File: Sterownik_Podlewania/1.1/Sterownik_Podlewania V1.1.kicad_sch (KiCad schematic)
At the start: 28 parts, among them J3 RJ45, J4 Conn_01x04_Socket, J5 RJ45, J8 RJ45, U1 ESP32-DEVKITC, U11 757, U5 757

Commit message: Pociągnięcie prawie wszystkich ścieżek, dodanie rezystorów do I2C 5V
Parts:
- added R12, R14: 4k7, Resistor_SMD:R_1206_3216Metric, symbol Device:R
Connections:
- net +5V: now also R12.1, R14.1
- net DS_WYJŚCIE: now also U1.9 (IO25); no longer U1.12 (IO14)
- net SCL_5V: now also R14.2
- net SDA_5V: now also R12.2

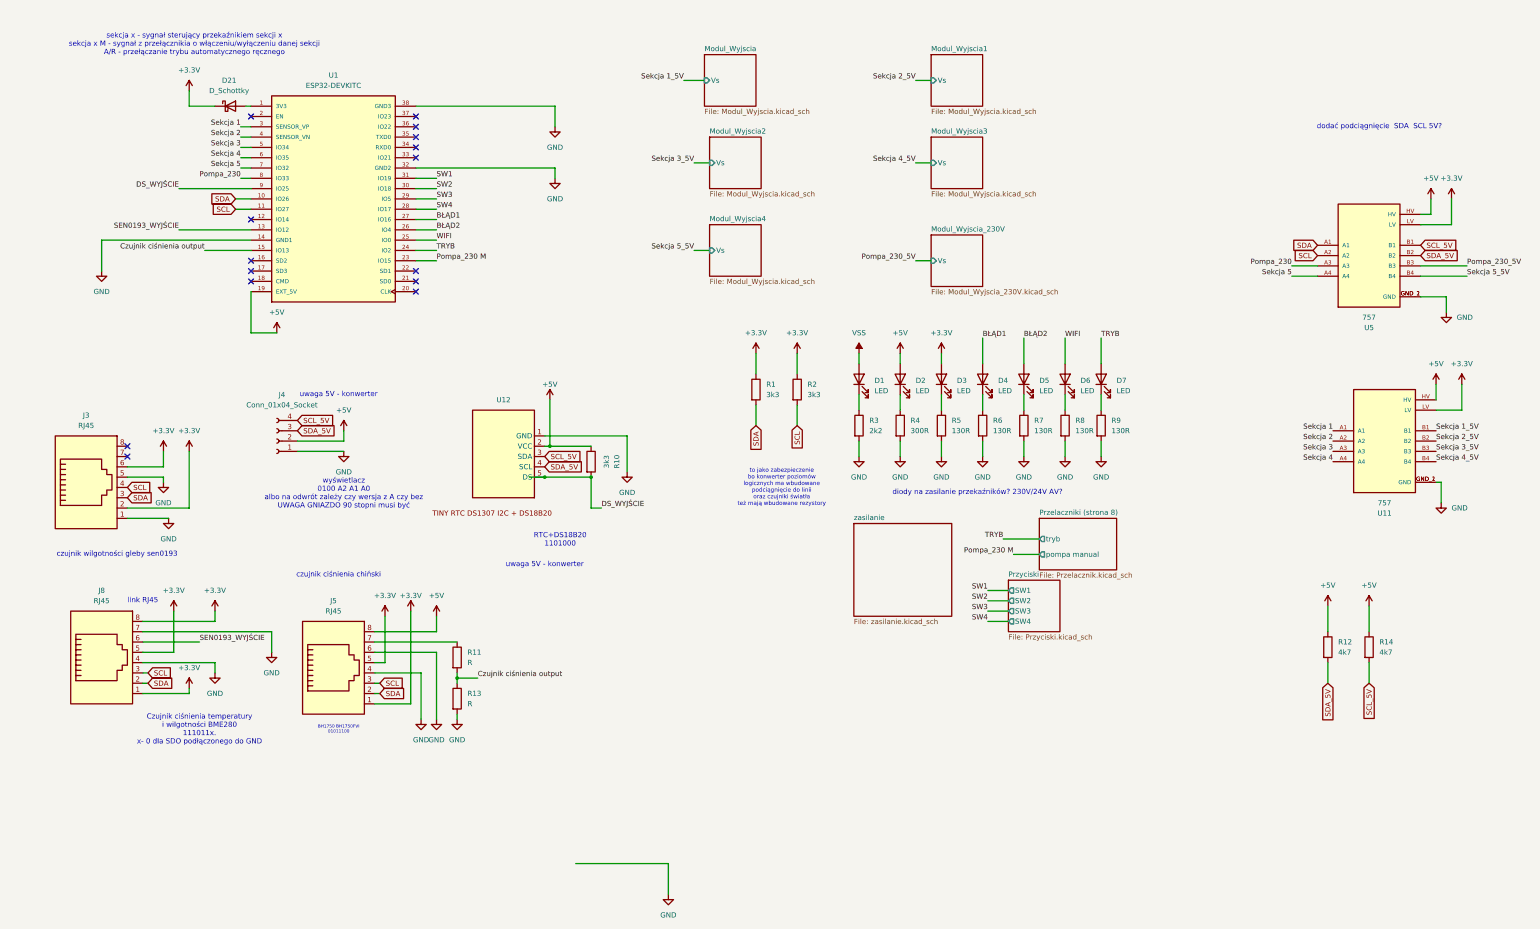
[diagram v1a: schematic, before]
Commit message: Poprawiono błędy połączeń SDA,SCL, dodno drugą magistralę I2C, pociągnięcie nowych ścieżek
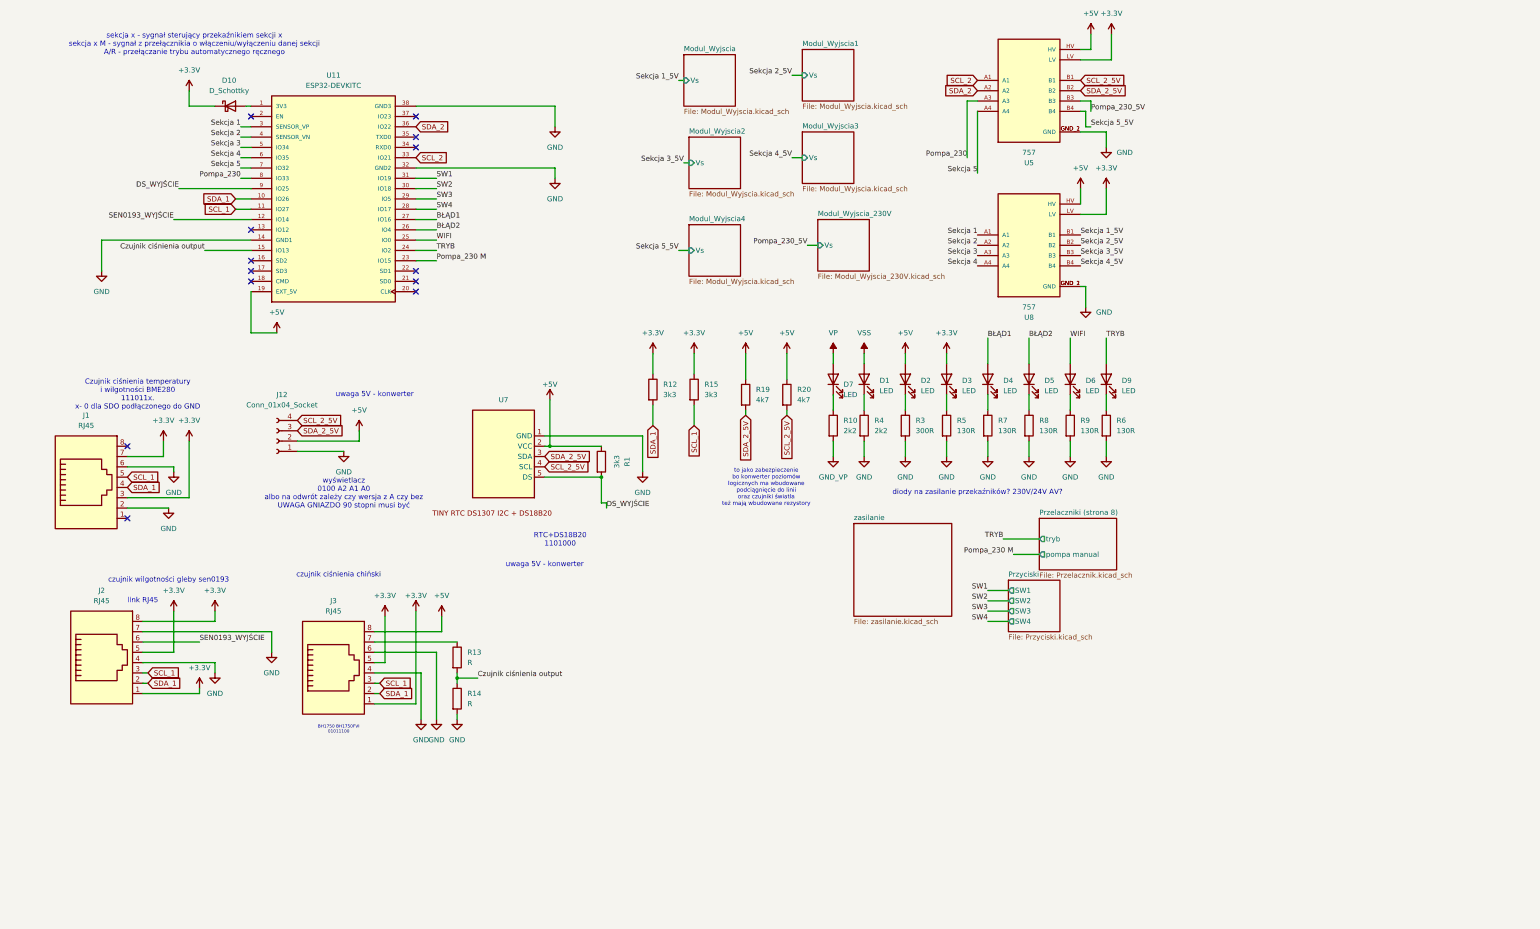
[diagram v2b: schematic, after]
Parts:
- removed U12: ~, RTC:RTC DS1307 + 32kb EEPROM 24C32 I2C, symbol RTC:TINY_RTC_DS1307
- added D7: LED, LED_SMD:LED_1206_3216Metric, symbol Device:LED
- added R10: 2k2, Resistor_SMD:R_1206_3216Metric, symbol Device:R
- added U7: ~, RTC:RTC DS1307 + 32kb EEPROM 24C32 I2C, symbol RTC:TINY_RTC_DS1307
- renumbered D21 to D10, D7 to D9, J3 to J1, J4 to J12, J8 to J2, J5 to J3, R10 to R1, R1 to R12, R11 to R13, R13 to R14, R2 to R15, R12 to R19, R14 to R20, R4 to R3, R3 to R4, R9 to R6, R6 to R7, R7 to R8, R8 to R9, U1 to U11, U11 to U8
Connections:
- net +3.3V: now also J1.3, J1.7; no longer J1.2, J1.6
- net +5V: now also U7.2 (VCC)
- net DS_WYJŚCIE: now also U7.5 (DS)
- net GND: now also J1.2, J1.6, U7.1 (GND); no longer J1.1, J1.5
- net SEN0193_WYJŚCIE: now also U11.12 (IO14); no longer U11.13 (IO12)
- net SCL_2: now reaches U11.33 (IO21)
- net SCL_2: now also U5.A1
- net SDA_2: now reaches U11.36 (IO22)
- net SDA_2: now also U5.A2
- net SCL renamed SCL_1
- net SCL_1: now also J1.5; no longer J1.4, U5.A2
- net SCL_5V renamed SCL_2_5V
- net SCL_2_5V: now also U7.4 (SCL)
- net SDA renamed SDA_1
- net SDA_1: now also J1.4; no longer J1.3, U5.A1
- net SDA_5V renamed SDA_2_5V
- net SDA_2_5V: now also U7.3 (SDA)
- new net: D7.1 (K), R10.1
- new net GND_VP: R10.2
- new net VP: D7.2 (A)
- no-connect marks 15 -> 13
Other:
- note removed: "dodać podciągnięcie SDA SCL 5V?"
- moved on the sheet: D1, D2, D3, D4, D5, D6, D9, R1, R12, R15, R19, R20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

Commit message: Poprawki schematu modułu zaworu, usunięcie przekaźnika, przygotowanie schematu zasilania
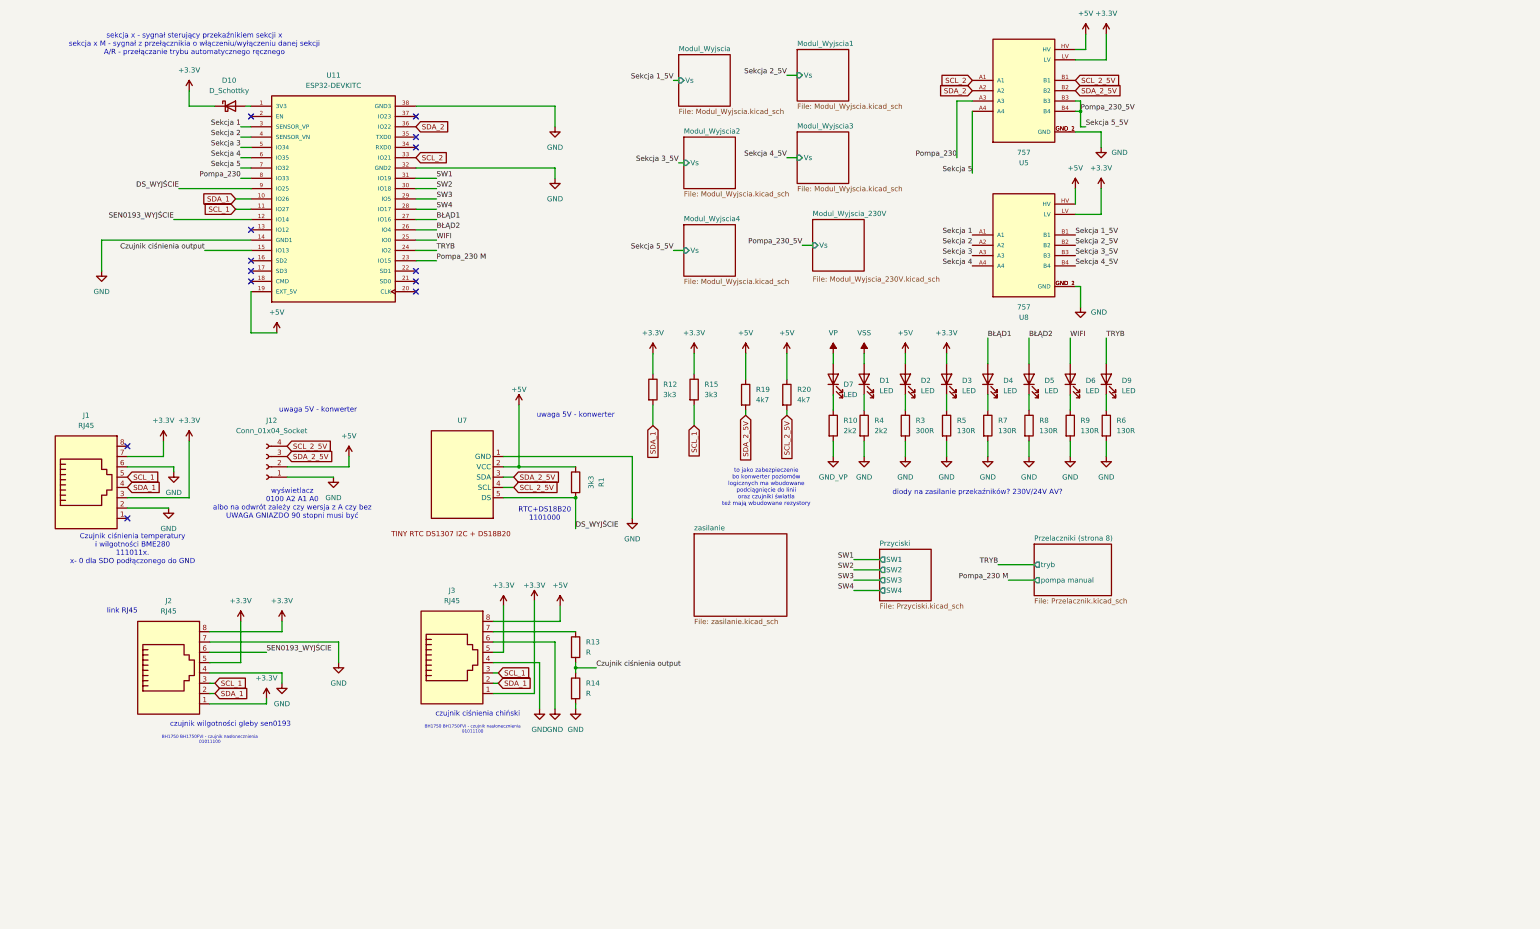
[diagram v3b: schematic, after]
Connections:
- net Sekcja 5_5V is gone; now on net Pompa_230_5V: U5.B4
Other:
- note added: "BH1750 BH1750FVI - czujnik nasłonecznienia 01011100"
- note removed: "BH1750 BH1750FVI 01011100"
- moved on the sheet: J12, J2, J3, R1, R13, R14, U5, U7, U8

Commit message: Usunięcie zewnętrzego zasilania 12 i stabilizatora napięcia, korekcja zasilania wzmacniacz operacyjny moduł zasilania
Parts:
- removed D1: LED, LED_SMD:LED_1206_3216Metric, symbol Device:LED
- removed R4: 2k2, Resistor_SMD:R_1206_3216Metric, symbol Device:R
- renumbered D10 to D1, D2 to D1, D4 to D2, D3 to D2, D5 to D4, D6 to D5, D7 to D6, D9 to D8, J12 to J3, J3 to J4, R5 to R10, R7 to R11, R8 to R12, R9 to R13, R6 to R14, R13 to R2, R14 to R3, R12 to R4, R15 to R5, R19 to R6, R20 to R7, R10 to R8, R3 to R9, U11 to U1, U7 to U2, U5 to U3, U8 to U4
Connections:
- net Pompa_230_5V: no longer U3.B4
- new net Sekcja 5_5V: U3.B4
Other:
- note added: "BH1750 BH1750FVI - czujnik światła I2C 01011100"
- note added: "to jako ewentualnosć do przytlutowania bo konwerter poziomów logicznych ma wbudowane podciągnięcie do linii oraz czujniki światła też mają wbudowane rezystory"
- note removed: "BH1750 BH1750FVI - czujnik nasłonecznienia 01011100"
- note removed: "to jako zabezpieczenie bo konwerter poziomów logicznych ma wbudowane podciągnięcie do linii oraz czujniki światła też mają wbudowane rezystory"
- moved on the sheet: D1, D2, D4, D5, D6, D8, R10, R11, R12, R13, R14, R8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

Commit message: Werja plików podesłana Mariuszkowi, dodane opisy i numeracja poprawna dla steronwika, w module poprawniono opis złącze ethernet
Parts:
- renumbered D8 to D11, D1 to D3, D2 to D6, D4 to D7, D5 to D8, D6 to D9, J3 to J12, J1 to J7, J2 to J8, J4 to J9, R9 to R1, R6 to R10, R7 to R11, R4 to R12, R5 to R13, R3 to R14, R2 to R15, R10 to R2, R11 to R3, R12 to R4, R13 to R5, R8 to R6, R14 to R8, R1 to R9, U1 to U10, U3 to U7, U2 to U8, U4 to U9
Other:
- note added: "sygnał manulanego włączenia pompy za pomocą przełącznika"
- note added: "tryb - ręczny/automatyczny"
- note removed: "diody na zasilanie przekaźników? 230V/24V AV?"
- note removed: "sekcja x - sygnał sterujący przekaźnikiem sekcji x sekcja x M - sygnał z przełącznikia o włączeniu/wyłączeniu danej sekcji A/R - przełączanie trybu automatycznego ręcznego"
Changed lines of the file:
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@@
 		)
 	)
-	(text "sekcja x - sygnał sterujący przekaźnikiem sekcji x\nsekcja x M - sygnał z przełącznikia o włączeniu/wyłączeniu danej sekcji\nA/R - przełączanie trybu automatycznego ręcznego"
+	(text "czujnik wilgotności gleby sen0193\n"
 		(exclude_from_sim no)
-		(at 50.8 21.59 0)
+		(at 59.69 189.23 0)
 		(effects
 			(font
 				(size 1.27 1.27)
 			)
+			(href "https://botland.com.pl/gravity-czujniki-pogodowe/10305-dfrobot-gravity-analogowy-czujnik-wilgotnosci-gleby-odporny-na-korozje-sen0193-6959420910434.html")
 		)
 	)
-	(text "czujnik wilgotności gleby sen0193\n"
+	(text "sygnał manulanego włączenia pompy\nza pomocą przełącznika\n"
 		(exclude_from_sim no)
-		(at 59.69 189.23 0)
+		(at 130.81 77.47 0)
 		(effects
 			(font
 				(size 1.27 1.27)
 			)
-			(href "https://botland.com.pl/gravity-czujniki-pogodowe/10305-dfrobot-gravity-analogowy-czujnik-wilgotnosci-gleby-odporny-na-korozje-sen0193-6959420910434.html")
 		)
 	)
-	(text "diody na zasilanie przekaźników? 230V/24V AV?"
+	(text "tryb - ręczny/automatyczny"
 		(exclude_from_sim no)
-		(at 243.84 132.08 0)
+		(at 130.81 71.12 0)
 		(effects
 			(font
@@
 	(text "to jako ewentualnosć do przytlutowania\nbo konwerter poziomów\nlogicznych ma wbudowane \npodciągnięcie do linii \noraz czujniki światła \nteż mają wbudowane rezystory"
 		(exclude_from_sim no)
-		(at 190.5 130.81 0)
+		(at 189.23 132.08 0)
 		(effects
 			(font
@@
 		(dnp no)
 		(fields_autoplaced yes)
-		(property "Reference" "D4"
+		(property "Reference" "D7"
 			(at 259.08 104.4574 90)
 			(effects
@@
 			(project "Sterownik_Podlewania"
 				(path "/a66bdf1f-0e2a-4cc5-beb1-605f2a3b9885"
-					(reference "D4")
+					(reference "D7")
 					(unit 1)
 				)
@@
 		(dnp no)
 		(fields_autoplaced yes)
-		(property "Reference" "R7"
+		(property "Reference" "R11"
 			(at 199.39 106.6799 0)
 			(effects
@@
 			(project "Sterownik_Podlewania V1.1"
 				(path "/a66bdf1f-0e2a-4cc5-beb1-605f2a3b9885"
-					(reference "R7")
+					(reference "R11")
 					(unit 1)
 				)
@@
 		(dnp no)
 		(fields_autoplaced yes)
-		(property "Reference" "J1"
+		(property "Reference" "J7"
 			(at 24.13 113.03 0)
 			(effects
@@
 			(project "Sterownik_Podlewania"
 				(path "/a66bdf1f-0e2a-4cc5-beb1-605f2a3b9885"
-					(reference "J1")
+					(reference "J7")
 					(unit 1)
 				)
@@
 		(on_board yes)
 		(dnp no)
-		(property "Reference" "J3"
+		(property "Reference" "J12"
 			(at 69.85 114.3 0)
 			(effects
@@
 			(project ""
 				(path "/a66bdf1f-0e2a-4cc5-beb1-605f2a3b9885"
-					(reference "J3")
+					(reference "J12")
 					(unit 1)
 				)
@@
 		(on_board yes)
 		(dnp no)
-		(property "Reference" "R1"
+		(property "Reference" "R9"
 			(at 151.13 129.54 90)
 			(effects
@@
 			(project ""
 				(path "/a66bdf1f-0e2a-4cc5-beb1-605f2a3b9885"
-					(reference "R1")
+					(reference "R9")
 					(unit 1)
 				)
@@
 		(dnp no)
 		(fields_autoplaced yes)
-		(property "Reference" "R14"
+		(property "Reference" "R8"
 			(at 276.86 114.2999 0)
 			(effects
@@
 			(project "Sterownik_Podlewania"
 				(path "/a66bdf1f-0e2a-4cc5-beb1-605f2a3b9885"
-					(reference "R14")
+					(reference "R8")
 					(unit 1)
 				)
@@
 		(on_board yes)
 		(dnp no)
-		(property "Reference" "R6"
+		(property "Reference" "R10"
 			(at 189.23 106.6799 0)
 			(effects
@@
 			(project "Sterownik_Podlewania V1.1"
 				(path "/a66bdf1f-0e2a-4cc5-beb1-605f2a3b9885"
-					(reference "R6")
+					(reference "R10")
 					(unit 1)
 				)
@@
 		(dnp no)
 		(fields_autoplaced yes)
-		(property "Reference" "R5"
+		(property "Reference" "R13"
 			(at 176.53 105.4099 0)
 			(effects
@@
 			(project "Sterownik_Podlewania"
 				(path "/a66bdf1f-0e2a-4cc5-beb1-605f2a3b9885"
-					(reference "R5")
+					(reference "R13")
 					(unit 1)
 				)
@@
 		(dnp no)
 		(fields_autoplaced yes)
-		(property "Reference" "R12"
+		(property "Reference" "R4"
 			(at 257.81 114.2999 0)
 			(effects
@@
 			(project "Sterownik_Podlewania"
 				(path "/a66bdf1f-0e2a-4cc5-beb1-605f2a3b9885"
-					(reference "R12")
+					(reference "R4")
 					(unit 1)
 				)
@@
 		(dnp no)
 		(fields_autoplaced yes)
-		(property "Reference" "R9"
+		(property "Reference" "R1"
 			(at 226.06 114.2999 0)
 			(effects
@@
 			(project "Sterownik_Podlewania"
 				(path "/a66bdf1f-0e2a-4cc5-beb1-605f2a3b9885"
-					(reference "R9")
+					(reference "R1")
 					(unit 1)
 				)
@@
 		(dnp no)
 		(fields_autoplaced yes)
-		(property "Reference" "D2"
+		(property "Reference" "D6"
 			(at 248.92 104.4574 90)
 			(effects
@@
 			(project "Sterownik_Podlewania"
 				(path "/a66bdf1f-0e2a-4cc5-beb1-605f2a3b9885"
-					(reference "D2")
+					(reference "D6")
 					(unit 1)
 				)
@@
 		(dnp no)
 		(fields_autoplaced yes)
-		(property "Reference" "U4"
+		(property "Reference" "U9"
 			(at 255.27 88.9 0)
 			(effects
@@
 			(project "Sterownik_Podlewania V1.1"
 				(path "/a66bdf1f-0e2a-4cc5-beb1-605f2a3b9885"
-					(reference "U4")
+					(reference "U9")
 					(unit 1)
 				)
@@
 		(dnp no)
 		(fields_autoplaced yes)
-		(property "Reference" "D8"
+		(property "Reference" "D11"
 			(at 278.13 104.4574 90)
 			(effects
@@
 			(project "Sterownik_Podlewania"
 				(path "/a66bdf1f-0e2a-4cc5-beb1-605f2a3b9885"
-					(reference "D8")
+					(reference "D11")
 					(unit 1)
 				)
@@
 		(dnp no)
 		(fields_autoplaced yes)
-		(property "Reference" "U1"
+		(property "Reference" "U10"
 			(at 85.09 29.21 0)
 			(effects
@@
 			(project ""
 				(path "/a66bdf1f-0e2a-4cc5-beb1-605f2a3b9885"
-					(reference "U1")
+					(reference "U10")
 					(unit 1)
 				)
@@
 		(on_board yes)
 		(dnp no)
-		(property "Reference" "R2"
+		(property "Reference" "R15"
 			(at 147.32 168.9099 0)
 			(effects
@@
 			(project "Sterownik_Podlewania V1.1"
 				(path "/a66bdf1f-0e2a-4cc5-beb1-605f2a3b9885"
-					(reference "R2")
+					(reference "R15")
 					(unit 1)
 				)
@@
 		(dnp no)
 		(fields_autoplaced yes)
-		(property "Reference" "D1"
+		(property "Reference" "D3"
 			(at 59.3725 30.48 0)
 			(effects
@@
 			(project "Sterownik_Podlewania"
 				(path "/a66bdf1f-0e2a-4cc5-beb1-605f2a3b9885"
-					(reference "D1")
+					(reference "D3")
 					(unit 1)
 				)
@@
 		(on_board yes)
 		(dnp no)
-		(property "Reference" "R13"
+		(property "Reference" "R5"
 			(at 267.97 114.2999 0)
 			(effects
@@
 			(project "Sterownik_Podlewania"
 				(path "/a66bdf1f-0e2a-4cc5-beb1-605f2a3b9885"
-					(reference "R13")
+					(reference "R5")
 					(unit 1)
 				)
@@
 		(dnp no)
 		(fields_autoplaced yes)
-		(property "Reference" "U3"
+		(property "Reference" "U7"
 			(at 255.27 50.8 0)
 			(effects
@@
 			(project ""
 				(path "/a66bdf1f-0e2a-4cc5-beb1-605f2a3b9885"
-					(reference "U3")
+					(reference "U7")
 					(unit 1)
 				)
@@
 		(dnp no)
 		(fields_autoplaced yes)
-		(property "Reference" "R10"
+		(property "Reference" "R2"
 			(at 237.49 114.2999 0)
 			(effects
@@
 			(project "Sterownik_Podlewania"
 				(path "/a66bdf1f-0e2a-4cc5-beb1-605f2a3b9885"
-					(reference "R10")
+					(reference "R2")
 					(unit 1)
 				)
@@
 		(on_board yes)
 		(dnp no)
-		(property "Reference" "U2"
+		(property "Reference" "U8"
 			(at 116.84 114.3 0)
 			(effects
@@
 			(project "Sterownik_Podlewania V1.1"
 				(path "/a66bdf1f-0e2a-4cc5-beb1-605f2a3b9885"
-					(reference "U2")
+					(reference "U8")
 					(unit 1)
 				)
@@
 		(on_board yes)
 		(dnp no)
-		(property "Reference" "D5"
+		(property "Reference" "D8"
 			(at 269.24 104.4574 90)
 			(effects
@@
 			(project "Sterownik_Podlewania"
 				(path "/a66bdf1f-0e2a-4cc5-beb1-605f2a3b9885"
-					(reference "D5")
+					(reference "D8")
 					(unit 1)
 				)
@@
 		(on_board yes)
 		(dnp no)
-		(property "Reference" "R4"
+		(property "Reference" "R12"
 			(at 166.37 105.4099 0)
 			(effects
@@
 			(project ""
 				(path "/a66bdf1f-0e2a-4cc5-beb1-605f2a3b9885"
-					(reference "R4")
+					(reference "R12")
 					(unit 1)
 				)
@@
 		(dnp no)
 		(fields_autoplaced yes)
-		(property "Reference" "R11"
+		(property "Reference" "R3"
 			(at 247.65 114.2999 0)
 			(effects
@@
 			(project "Sterownik_Podlewania"
 				(path "/a66bdf1f-0e2a-4cc5-beb1-605f2a3b9885"
-					(reference "R11")
+					(reference "R3")
 					(unit 1)
 				)
@@
 		(dnp no)
 		(fields_autoplaced yes)
-		(property "Reference" "J4"
+		(property "Reference" "J9"
 			(at 114.3 156.21 0)
 			(effects
@@
 			(project "Sterownik_Podlewania"
 				(path "/a66bdf1f-0e2a-4cc5-beb1-605f2a3b9885"
-					(reference "J4")
+					(reference "J9")
 					(unit 1)
 				)
@@
 		(dnp no)
 		(fields_autoplaced yes)
-		(property "Reference" "R3"
+		(property "Reference" "R14"
 			(at 147.32 179.0699 0)
 			(effects
@@
 			(project "Sterownik_Podlewania V1.1"
 				(path "/a66bdf1f-0e2a-4cc5-beb1-605f2a3b9885"
-					(reference "R3")
+					(reference "R14")
 					(unit 1)
 				)
@@
 		(dnp no)
 		(fields_autoplaced yes)
-		(property "Reference" "R8"
+		(property "Reference" "R6"
 			(at 214.63 114.2999 0)
 			(effects
@@
 			(project "Sterownik_Podlewania V1.1"
 				(path "/a66bdf1f-0e2a-4cc5-beb1-605f2a3b9885"
-					(reference "R8")
+					(reference "R6")
 					(unit 1)
 				)
@@
 		(dnp no)
 		(fields_autoplaced yes)
-		(property "Reference" "J2"
+		(property "Reference" "J8"
 			(at 44.45 158.75 0)
 			(effects
@@
 			(project ""
 				(path "/a66bdf1f-0e2a-4cc5-beb1-605f2a3b9885"
-					(reference "J2")
+					(reference "J8")
 					(unit 1)
 				)
@@
 		(on_board yes)
 		(dnp no)
-		(property "Reference" "D6"
+		(property "Reference" "D9"
 			(at 214.63 105.41 90)
 			(effects
@@
 			(project "Sterownik_Podlewania V1.1"
 				(path "/a66bdf1f-0e2a-4cc5-beb1-605f2a3b9885"
-					(reference "D6")
+					(reference "D9")
 					(unit 1)
 				)
